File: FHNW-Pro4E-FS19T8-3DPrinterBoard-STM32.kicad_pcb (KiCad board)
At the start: 4 copper layers, 158 x 95 mm, 264 parts, among them J101 Screw_Terminal_01x02, J201 Micro_SD_Card_Det, J202 Conn_02x05_Odd_Even, J203 Conn_02x20_Odd_Even, J204 Conn_ARM_JTAG_SWD_10, J401 Conn_01x02, J402 Conn_01x02, J403 Screw_Terminal_01x02, J404 Conn_01x02, J405 Conn_01x02, J406 Screw_Terminal_01x02, J407 Conn_01x02, J408 Conn_01x02, J409 Conn_01x02, J410 Conn_01x02, J411 Conn_01x02, J504 USB_C_Receptacle, J601 B4B-XH-A, J602 B4B-XH-A, J603 B4B-XH-A, J604 B4B-XH-A, J605 Conn_01x03, J606 Conn_01x03, Q1 2N3904, Q2 2N3904, SW201 SW_Push, SW202 SW_Push, SW203 SW_Push, SW301 SW_Push, SW302 SW_Push, T101 BUK963R3-60E, T401 PMV40UN2, T402 BUK963R3-60E, T403 BUK963R3-60E, T404 PMV40UN2, T405 PMV40UN2, U1 USBLC6-2SC6, U101 LM2675M-3.3, U102 LM2675M-5, U201 STM32F103ZETx, U202 NTS0104PW-Q100J, U203 NTS0104PW-Q100J, U301 ESP32-WROOM-32, U502 FT2232D, U601 TMC2660, U602 TMC2660, U603 TMC2660, U604 TMC2660, X201 SG-210STF, X501 SG5032CCN-6.000000M-HJGA3

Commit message: finished up for final review
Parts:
- removed C105, C221: 100n, Capacitors_SMD:C_0603
- removed R225: 0R, Resistors_SMD:R_0603
- removed R232: 10k, Resistors_SMD:R_0603
- added D607: BAT54S, Package_TO_SOT_SMD:SOT-23, F.Cu at (224.2, 93.3)
- added D608: BAT54S, Package_TO_SOT_SMD:SOT-23, F.Cu at (224.2, 83.2)
- added R220: 0R, Resistors_SMD:R_0603, F.Cu at (209.9, 57.9)
- added R221: 0R, Resistors_SMD:R_0603, F.Cu at (211.5, 73.0)
- moved C219 88.4 mm to (197.5, 94.0), turned to 270 degrees
- moved C508 83.0 mm to (212.7, 80.0)
- moved C218 61.5 mm to (198.1, 58.4), turned to 270 degrees
- moved C220 59.8 mm to (203.8, 24.1), turned to 270 degrees
- moved R231 57.3 mm to (217.8, 52.7), turned to 90 degrees
- moved R230 50.8 mm to (219.7, 52.7), turned to 90 degrees
- moved R237 9.94 mm to (211.5, 71.1), turned to 0 degrees
- moved R229 6.84 mm to (207.0, 73.0), turned to 0 degrees
- moved R227 6.38 mm to (207.0, 71.1), turned to 0 degrees
- moved J605 2.84 mm to (227.3, 92.1)
- moved J606 2.62 mm to (227.3, 81.9)
- moved R416 1.88 mm to (113.4, 35.8)
- moved R422 1.88 mm to (113.4, 33.9)
- moved D401 1.73 mm to (110.4, 35.8)
- moved C208 1.35 mm to (166.8, 65.2)
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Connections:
- J203 pad 18: ES_DIR -> E2_DIR
- R227 pad 1: /appendix_STM32F103/STM32_NRST -> JTAG_TRST
- R227 pad 2: NRST -> JTAG_RESET
- R229 pad 2: JTAG_TRST -> JTAG_RESET
- R237 pad 1: /appendix_STM32F103/STM32_BOOT_0 -> /appendix_STM32F103/STM_BOOT0
- U201 pad 10: Net-(U201-Pad10) -> E3_END_FIL
- U201 pad 114: Net-(U201-Pad114) -> E3_STEP
- U201 pad 115: Net-(U201-Pad115) -> E2_DIR
- U201 pad 122: Net-(U201-Pad122) -> /appendix_SENSORS_POWER/SERVO_1
- U201 pad 123: Net-(U201-Pad123) -> /appendix_SENSORS_POWER/SERVO_2
- U201 pad 124: Net-(U201-Pad124) -> E3_DIR
- U201 pad 125: Net-(U201-Pad125) -> E2_EN
- U201 pad 126: Net-(U201-Pad126) -> E2_STALL
- U201 pad 127: Net-(U201-Pad127) -> E3_STALL
- U201 pad 128: Net-(U201-Pad128) -> E3_EN
- U201 pad 129: Net-(U201-Pad129) -> E2_END_FIL
- U201 pad 134: NRST -> JTAG_TRST
- U201 pad 140: LCD_ENC_B -> LCD_ENC_A
- U201 pad 141: LCD_ENC_A -> LCD_ENC_B
- U201 pad 20: Net-(U201-Pad20) -> E3_ADC_TEMP
- U201 pad 21: Net-(U201-Pad21) -> ADC_TEMP_EXT
- U201 pad 22: Net-(U201-Pad22) -> E2_ADC_TEMP
- U201 pad 60: Net-(U201-Pad60) -> GPIO_EXT_3
- U201 pad 63: Net-(U201-Pad63) -> E2_HOTEND
- U201 pad 64: Net-(U201-Pad64) -> GPIO_EXT_2
- U201 pad 65: Net-(U201-Pad65) -> E2_FAN2
- U201 pad 66: Net-(U201-Pad66) -> GPIO_EXT_1
- U201 pad 67: Net-(U201-Pad67) -> E2_FAN1
- U201 pad 68: Net-(U201-Pad68) -> FAN_EXT
- U201 pad 77: Net-(U201-Pad77) -> GPIO_EXT_0
- U201 pad 78: Net-(U201-Pad78) -> E2_CS
- U201 pad 79: Net-(U201-Pad79) -> E3_CS
- U201 pad 85: Net-(U201-Pad85) -> E2_STEP
- U203 pad 3: LCD_ENC_A -> LCD_ENC_B
- U203 pad 4: LCD_ENC_B -> LCD_ENC_A
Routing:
- net Net-(F401-Pad1): track 44.1 -> 185.6 mm
- net E3_CS: track 0.00 -> 89.6 mm, vias 0 -> 1
- net GPIO_EXT_0: track 0.00 -> 89.1 mm, vias 0 -> 1
- net E2_CS: track 0.00 -> 86.3 mm, vias 0 -> 1
- net GPIO_EXT_1: track 0.00 -> 83.1 mm, vias 0 -> 1
- net FAN_EXT: track 0.00 -> 82.9 mm, vias 0 -> 1
- net E2_FAN1: track 0.00 -> 82.4 mm, vias 0 -> 1
- net E2_HOTEND: track 0.00 -> 81.7 mm, vias 0 -> 1
- net GPIO_EXT_3: track 0.00 -> 81.1 mm, vias 0 -> 1
- net E2_STEP: track 0.00 -> 80.4 mm, vias 0 -> 1
- net GPIO_EXT_2: track 0.00 -> 79.5 mm, vias 0 -> 1
- net E2_FAN2: track 0.00 -> 77.6 mm, vias 0 -> 1
- net ADC_TEMP_EXT: track 0.00 -> 74.6 mm, vias 0 -> 1
- net E3_ADC_TEMP: track 0.00 -> 73.9 mm, vias 0 -> 1
- net E2_ADC_TEMP: track 0.00 -> 73.5 mm, vias 0 -> 1
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- added copper zone on B.Cu, net (none)
- added copper zone on F.Cu, net (none)
- added copper zone on In2.Cu, net +3V3
- added copper zone on In1.Cu, net GND
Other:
- net class high current added: clearance 0.2, trace_width 2.5, via_dia 1, via_drill 0.5
- board text added: "BTN ESP"
- board text added: "BTN1"
- board text added: "BTN2"
- board text added: "ESP32"
- board text added: "RST ESP"
- board text added: "RST STM"
- board text added: "SERVO1"
- board text added: "STM32"
- board text removed: "OPTIONS"
- board text removed: "RESET"
- board text removed: "RST"

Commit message: fixed minor layout stuff with mueller
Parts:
- added R222: 0R, Resistors_SMD:R_0603, F.Cu at (209.0, 56.1)
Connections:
- U201 pad 31: Net-(U201-Pad31) -> GND
- U201 pad 32: Net-(U201-Pad32) -> +3.3VA
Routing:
- net Net-(R222-Pad2): track 0.00 -> 18.0 mm, vias 0 -> 2
- net Net-(U201-Pad100): track 11.3 -> 0.00 mm, vias 1 -> 0
- net /appendix_SENSORS_POWER/Bed_pwr: track 93.0 -> 99.0 mm, vias 6 -> 9
- net LCD_Reset: track 3.75 -> 5.98 mm
- net +3.3VA: track 81.5 -> 82.0 mm
- net GND: track 500.2 -> 500.7 mm, vias 100 -> 110
- net /appendix_SENSORS_POWER/E1_pwr: vias 6 -> 7
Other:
- board text added: "FHNW P4E FS19T8 3D Printer - 2019.04.24"

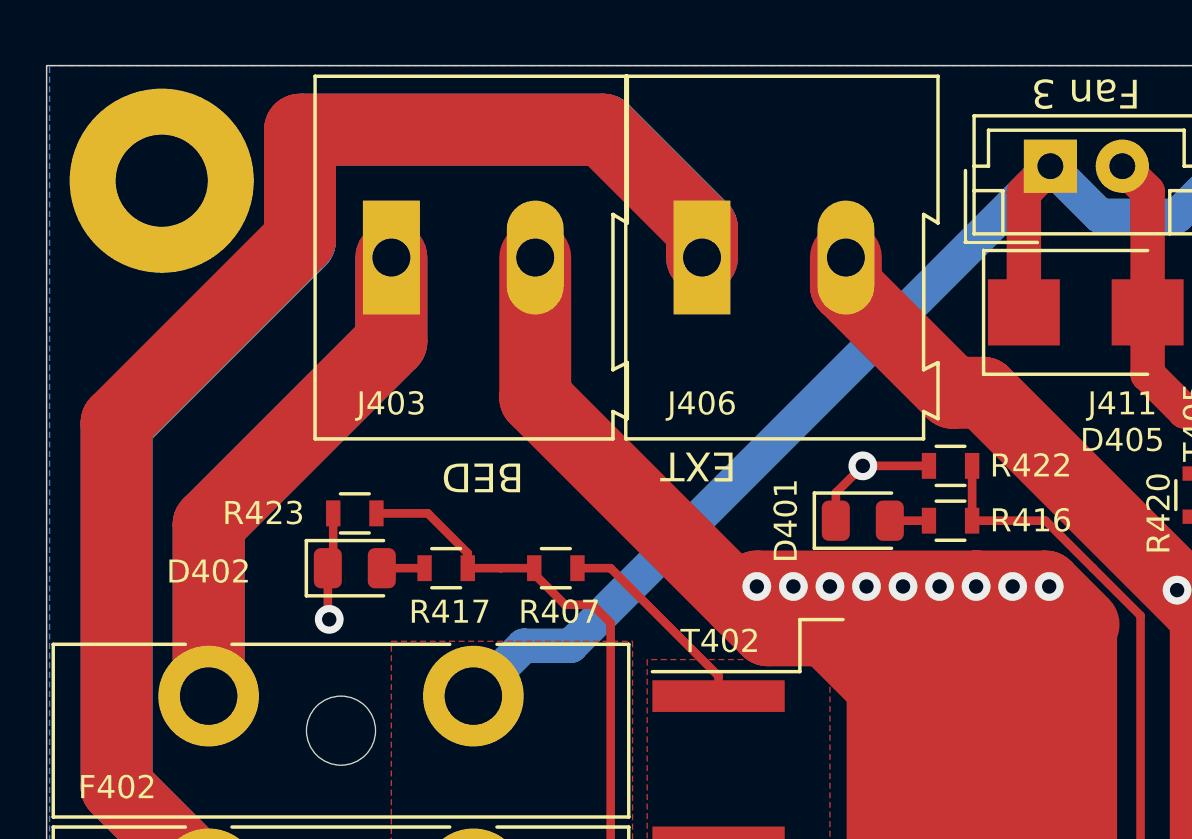
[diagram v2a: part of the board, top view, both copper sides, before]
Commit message: changed screw terminal for bed/ext
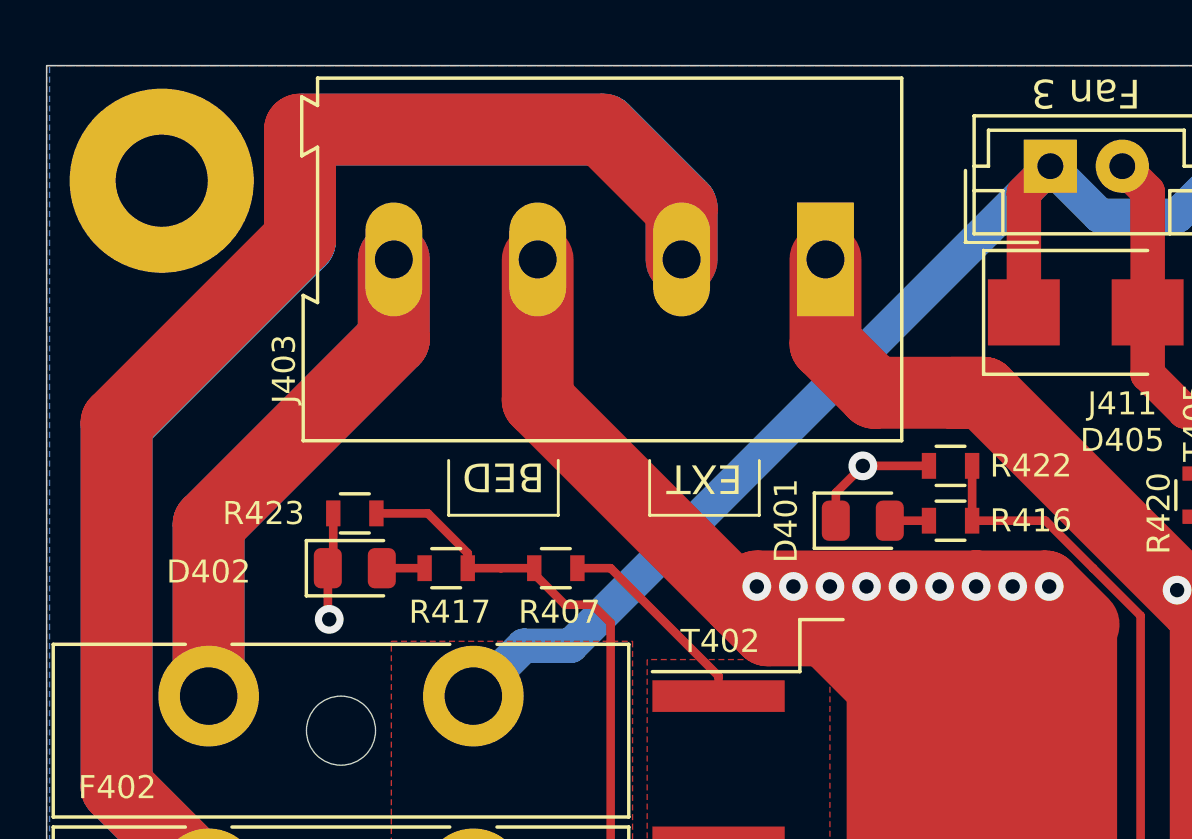
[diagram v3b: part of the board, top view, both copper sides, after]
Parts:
- removed J406: Screw_Terminal_01x02, Connectors_Terminal_Blocks:TerminalBlock_Altech_AK300-2_P5.00mm
- C217: value 10u -> 1u
- J403: value Screw_Terminal_01x02 -> Screw_Terminal_01x04; footprint Connectors_Terminal_Blocks:TerminalBlock_Altech_AK300-2_P5.00mm -> Connectors_Terminal_Blocks:TerminalBlock_Altech_AK300-4_P5.00mm
- moved J403 15.1 mm to (109.1, 26.7), turned to 180 degrees
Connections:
- J403 pad 1: Net-(F402-Pad1) -> /appendix_SENSORS_POWER/E1_pwr
- J403 pad 2: /appendix_SENSORS_POWER/Bed_pwr -> Net-(F401-Pad1)
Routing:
- net /appendix_SENSORS_POWER/E1_pwr: track 81.2 -> 87.6 mm
- net Net-(F401-Pad1): track 185.6 -> 184.8 mm

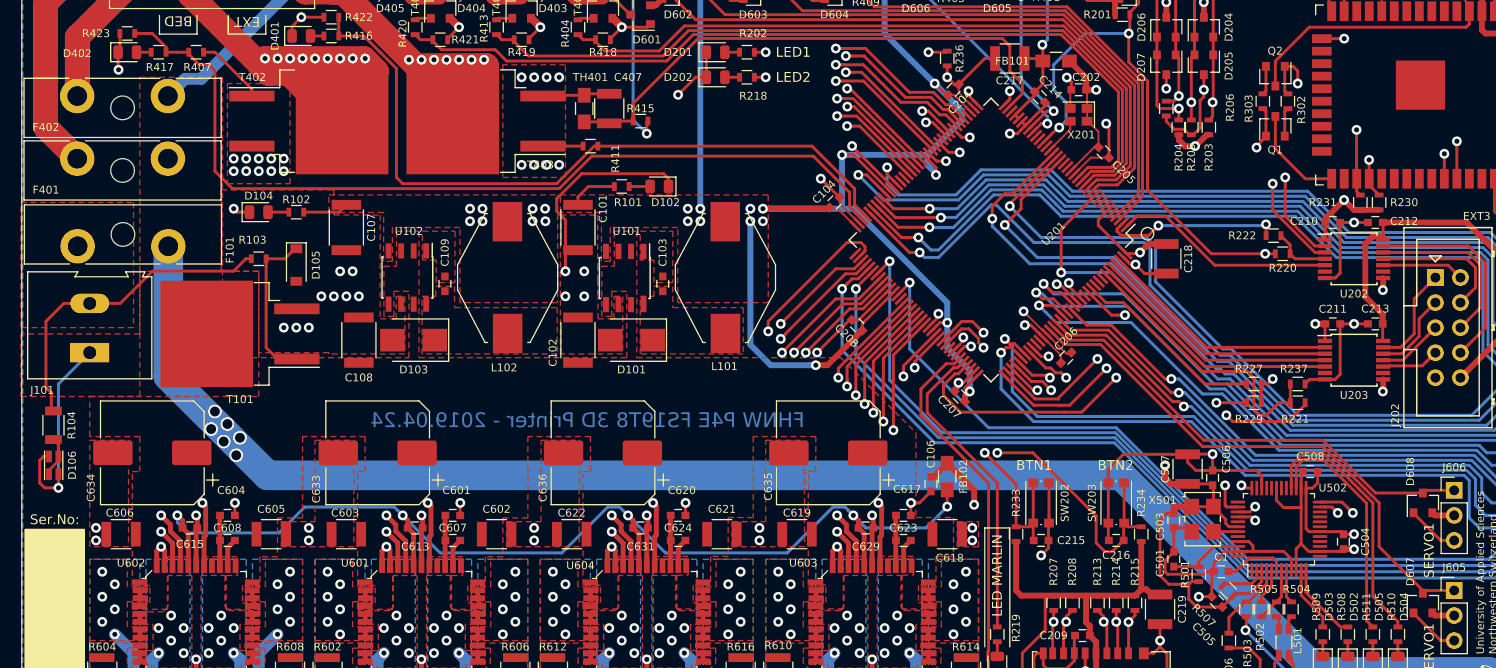
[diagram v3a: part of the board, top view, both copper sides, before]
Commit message: changed Layout to use all Interrupt Pins
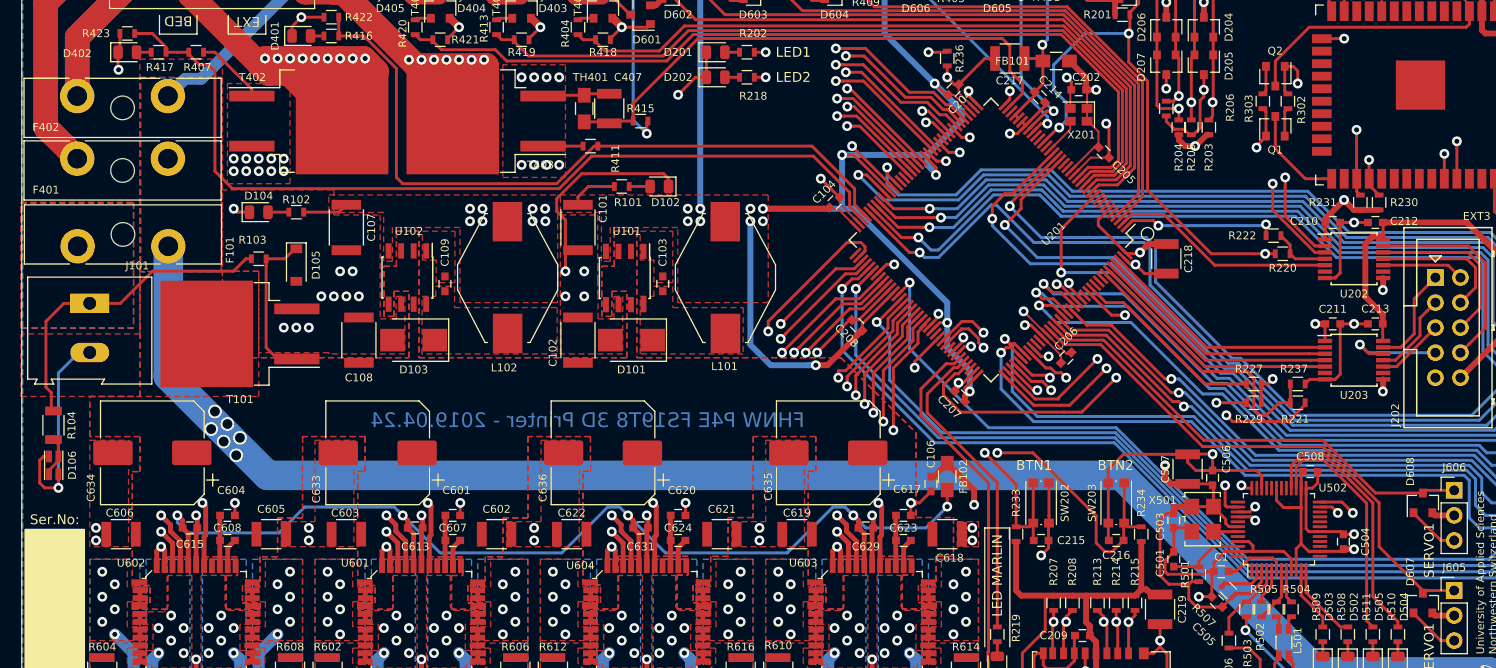
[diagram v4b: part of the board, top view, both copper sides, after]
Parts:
- moved J101 5.01 mm to (88.9, 62.9), turned to 270 degrees
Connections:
- J101 pad 1: /24V_GND -> /24V_IN
- J101 pad 2: /24V_IN -> /24V_GND
- U201 pad 1: LCD_ENC_BTN -> Net-(R222-Pad2)
- U201 pad 139: LCD_CS -> LCD_ENC_A
- U201 pad 140: LCD_ENC_A -> LCD_ENC_B
- U201 pad 141: LCD_ENC_B -> LCD_CS
- U201 pad 2: Net-(R222-Pad2) -> LCD_ENC_BTN
- U201 pad 79: E3_CS -> BTN_USER_1
- U201 pad 86: Net-(U201-Pad86) -> E3_CS
- U201 pad 96: BTN_USER_1 -> Net-(U201-Pad96)
- U203 pad 10: EXP3_LCD_CS -> EXP3_LCD_Encoder_A
- U203 pad 11: EXP3_LCD_Encoder_A -> EXP3_LCD_Encoder_B
- U203 pad 12: EXP3_LCD_Encoder_B -> EXP3_LCD_CS
- U203 pad 3: LCD_ENC_B -> LCD_CS
- U203 pad 4: LCD_ENC_A -> LCD_ENC_B
- U203 pad 5: LCD_CS -> LCD_ENC_A
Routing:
- net BTN_USER_1: track 33.7 -> 41.8 mm
- net EXP3_LCD_CS: track 5.89 -> 10.7 mm, vias 0 -> 1
- net E3_CS: track 89.6 -> 85.5 mm
- net Net-(R222-Pad2): track 18.0 -> 15.8 mm
- net LCD_CS: track 25.9 -> 25.0 mm
- net /24V_GND: track 21.9 -> 22.6 mm
- added copper zone on B.Cu, net +24V
- added copper zone on In1.Cu, net +24V
- added copper zone on In2.Cu, net +24V
- added copper zone on B.Cu, net /24V_IN
- added copper zone on In1.Cu, net /24V_IN
- added copper zone on In2.Cu, net /24V_IN

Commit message: fixed last minor issues
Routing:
- net Net-(U201-Pad44): track 2.05 -> 0.00 mm, vias 1 -> 0
- net GND: track 500.7 -> 502.2 mm
- net +3V3: track 742.2 -> 741.0 mm
